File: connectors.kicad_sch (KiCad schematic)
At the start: 10 parts, among them J1 CE_Jumper, J2 LDO_EN, J3 Conn_01x05_Pin, J4 JST_VH_B2P_3.96mm, J5 JST_VH_B2P_3.96mm, J7 Thermistor_1, J8 Thermistor_2

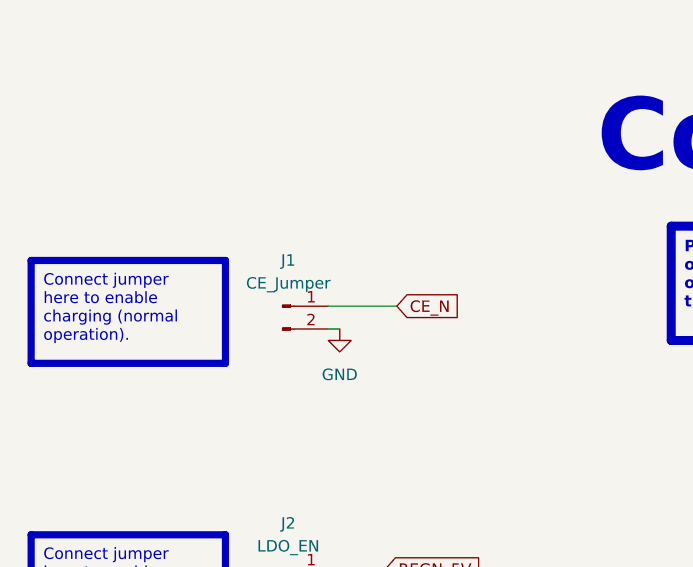
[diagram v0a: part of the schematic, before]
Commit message: Replace jumper to force BOM updated
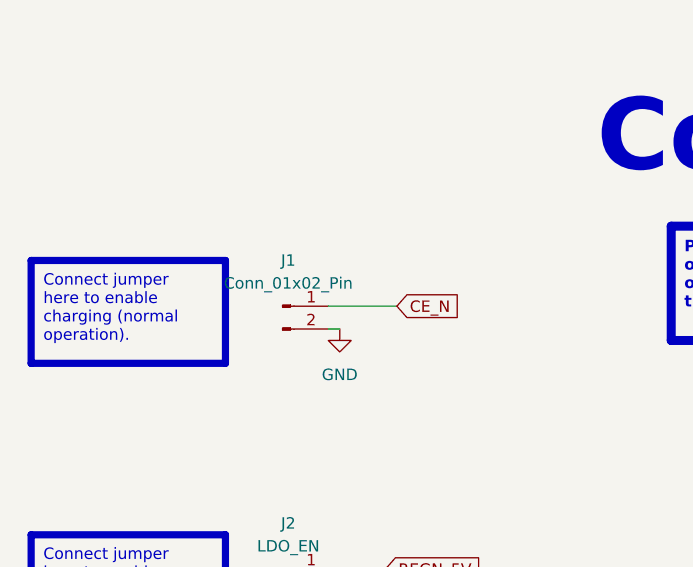
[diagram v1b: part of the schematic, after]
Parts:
- J1: value CE_Jumper -> Conn_01x02_Pin
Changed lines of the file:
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@@
-	)
-	(symbol
-		(lib_id "Connector:Conn_01x02_Pin")
-		(at 76.2 48.26 0)
-		(unit 1)
-		(exclude_from_sim no)
-		(in_bom yes)
-		(on_board yes)
-		(dnp no)
-		(fields_autoplaced yes)
-		(property "Reference" "J1"
-			(at 76.835 43.18 0)
-			(effects
-				(font
-					(size 1.27 1.27)
-				)
-			)
-		)
-		(property "Value" "CE_Jumper"
-			(at 76.835 45.72 0)
-			(effects
-				(font
-					(size 1.27 1.27)
-				)
-			)
-		)
-		(property "Footprint" "Connector_PinHeader_2.54mm:PinHeader_1x02_P2.54mm_Vertical"
-			(at 76.2 48.26 0)
-			(effects
-				(font
-					(size 1.27 1.27)
-				)
-				(hide yes)
-			)
-		)
-		(property "Datasheet" "~"
-			(at 76.2 48.26 0)
-			(effects
-				(font
-					(size 1.27 1.27)
-				)
-				(hide yes)
-			)
-		)
-		(property "Description" "Generic connector, single row, 01x02, script generated"
-			(at 76.2 48.26 0)
-			(effects
-				(font
-					(size 1.27 1.27)
-				)
-				(hide yes)
-			)
-		)
-		(pin "2"
-		)
-		(pin "1"
-		)
-		(instances
-			(project "solar_smart_station"
-				(path "/f9e05184-c88b-4a88-ae9c-ab2bdb32be7c/c5103ceb-5325-4a84-a025-9638a412984e/ae8d0caf-6898-4dee-88e6-fcc8a5387577"
-					(reference "J1")
-					(unit 1)
-				)
-			)
-		)
 	)
 	(symbol
@@
 					(unit 1)
 				)
+			)
+		)
+	)
+	(symbol
+		(lib_id "Connector:Conn_01x02_Pin")
+		(at 76.2 48.26 0)
+		(unit 1)
+		(exclude_from_sim no)
+		(in_bom yes)
+		(on_board yes)
+		(dnp no)
+		(fields_autoplaced yes)
+		(property "Reference" "J1"
+			(at 76.835 43.18 0)
+			(effects
+				(font
+					(size 1.27 1.27)
+				)
+			)
+		)
+		(property "Value" "Conn_01x02_Pin"
+			(at 76.835 45.72 0)
+			(effects
+				(font
+					(size 1.27 1.27)
+				)
+			)
+		)
+		(property "Footprint" "Connector_PinHeader_2.54mm:PinHeader_1x02_P2.54mm_Vertical"
+			(at 76.2 48.26 0)
+			(effects
+				(font
+					(size 1.27 1.27)
+				)
+				(hide yes)
+			)
+		)
+		(property "Datasheet" "~"
+			(at 76.2 48.26 0)
+			(effects
+				(font
+					(size 1.27 1.27)
+				)
+				(hide yes)
+			)
+		)
+		(property "Description" "Generic connector, single row, 01x02, script generated"
+			(at 76.2 48.26 0)
+			(effects
+				(font
+					(size 1.27 1.27)
+				)
+				(hide yes)
+			)
+		)
+		(pin "2"
+		)
+		(pin "1"
+		)
+		(instances
+			(project ""
+				(path "/f9e05184-c88b-4a88-ae9c-ab2bdb32be7c/c5103ceb-5325-4a84-a025-9638a412984e/ae8d0caf-6898-4dee-88e6-fcc8a5387577"
+					(reference "J1")
+					(unit 1)
+				)

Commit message: Finish checking - Ready for 1st release
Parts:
- renumbered J7 to J4, J8 to J5, J4 to JST1, J5 to JST2
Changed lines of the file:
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@@
 		(on_board yes)
 		(dnp no)
-		(property "Reference" "J8"
+		(property "Reference" "J5"
 			(at 184.785 110.49 0)
 			(effects
@@
 			(project "solar_smart_station"
 				(path "/f9e05184-c88b-4a88-ae9c-ab2bdb32be7c/c5103ceb-5325-4a84-a025-9638a412984e/ae8d0caf-6898-4dee-88e6-fcc8a5387577"
-					(reference "J8")
+					(reference "J5")
 					(unit 1)
 				)
@@
 		(dnp no)
 		(fields_autoplaced yes)
-		(property "Reference" "J5"
+		(property "Reference" "JST2"
 			(at 186.69 63.4999 0)
 			(effects
@@
 			(project "solar_smart_station"
 				(path "/f9e05184-c88b-4a88-ae9c-ab2bdb32be7c/c5103ceb-5325-4a84-a025-9638a412984e/ae8d0caf-6898-4dee-88e6-fcc8a5387577"
-					(reference "J5")
+					(reference "JST2")
 					(unit 1)
 				)
@@
 		(dnp no)
 		(fields_autoplaced yes)
-		(property "Reference" "#PWR045"
+		(property "Reference" "#PWR046"
 			(at 180.34 72.39 0)
 			(effects
@@
 			(project "solar_smart_station"
 				(path "/f9e05184-c88b-4a88-ae9c-ab2bdb32be7c/c5103ceb-5325-4a84-a025-9638a412984e/ae8d0caf-6898-4dee-88e6-fcc8a5387577"
-					(reference "#PWR045")
+					(reference "#PWR046")
 					(unit 1)
 				)
@@
 		(on_board yes)
 		(dnp no)
-		(property "Reference" "J7"
+		(property "Reference" "J4"
 			(at 184.785 97.79 0)
 			(effects
@@
 			(project "solar_smart_station"
 				(path "/f9e05184-c88b-4a88-ae9c-ab2bdb32be7c/c5103ceb-5325-4a84-a025-9638a412984e/ae8d0caf-6898-4dee-88e6-fcc8a5387577"
-					(reference "J7")
+					(reference "J4")
 					(unit 1)
 				)
@@
 		(dnp no)
 		(fields_autoplaced yes)
-		(property "Reference" "#PWR039"
+		(property "Reference" "#PWR041"
 			(at 82.55 57.15 0)
 			(effects
@@
 			(project "solar_smart_station"
 				(path "/f9e05184-c88b-4a88-ae9c-ab2bdb32be7c/c5103ceb-5325-4a84-a025-9638a412984e/ae8d0caf-6898-4dee-88e6-fcc8a5387577"
-					(reference "#PWR039")
+					(reference "#PWR041")
 					(unit 1)
 				)
@@
 		(dnp no)
 		(fields_autoplaced yes)
-		(property "Reference" "#PWR044"
+		(property "Reference" "#PWR045"
 			(at 180.34 54.61 0)
 			(effects
@@
 			(project "solar_smart_station"
 				(path "/f9e05184-c88b-4a88-ae9c-ab2bdb32be7c/c5103ceb-5325-4a84-a025-9638a412984e/ae8d0caf-6898-4dee-88e6-fcc8a5387577"
-					(reference "#PWR044")
+					(reference "#PWR045")
 					(unit 1)
 				)
@@
 		(dnp no)
 		(fields_autoplaced yes)
-		(property "Reference" "#PWR040"
+		(property "Reference" "#PWR042"
 			(at 152.4 49.53 0)
 			(effects
@@
 			(project "solar_smart_station"
 				(path "/f9e05184-c88b-4a88-ae9c-ab2bdb32be7c/c5103ceb-5325-4a84-a025-9638a412984e/ae8d0caf-6898-4dee-88e6-fcc8a5387577"
-					(reference "#PWR040")
+					(reference "#PWR042")
 					(unit 1)
 				)
@@
 		(dnp no)
 		(fields_autoplaced yes)
-		(property "Reference" "#PWR041"
+		(property "Reference" "#PWR047"
 			(at 209.55 50.8 0)
 			(effects
@@
 			(project "solar_smart_station"
 				(path "/f9e05184-c88b-4a88-ae9c-ab2bdb32be7c/c5103ceb-5325-4a84-a025-9638a412984e/ae8d0caf-6898-4dee-88e6-fcc8a5387577"
-					(reference "#PWR041")
+					(reference "#PWR047")
 					(unit 1)
 				)
@@
 		(dnp no)
 		(fields_autoplaced yes)
-		(property "Reference" "#PWR025"
+		(property "Reference" "#PWR039"
 			(at 60.96 138.43 0)
 			(effects
@@
 			(project "solar_smart_station"
 				(path "/f9e05184-c88b-4a88-ae9c-ab2bdb32be7c/c5103ceb-5325-4a84-a025-9638a412984e/ae8d0caf-6898-4dee-88e6-fcc8a5387577"
-					(reference "#PWR025")
+					(reference "#PWR039")
 					(unit 1)
 				)
@@
 		(on_board yes)
 		(dnp no)
-		(property "Reference" "#PWR047"
+		(property "Reference" "#PWR040"
 			(at 60.96 166.37 0)
 			(effects
@@
 			(project "solar_smart_station"
 				(path "/f9e05184-c88b-4a88-ae9c-ab2bdb32be7c/c5103ceb-5325-4a84-a025-9638a412984e/ae8d0caf-6898-4dee-88e6-fcc8a5387577"
-					(reference "#PWR047")
+					(reference "#PWR040")
 					(unit 1)
 				)
@@
 		(dnp no)
 		(fields_autoplaced yes)
-		(property "Reference" "#FLG03"
+		(property "Reference" "#FLG04"
 			(at 81.28 88.265 0)
 			(effects
@@
 			(project "solar_smart_station"
 				(path "/f9e05184-c88b-4a88-ae9c-ab2bdb32be7c/c5103ceb-5325-4a84-a025-9638a412984e/ae8d0caf-6898-4dee-88e6-fcc8a5387577"
-					(reference "#FLG03")
+					(reference "#FLG04")
 					(unit 1)
 				)
@@
 		(dnp no)
 		(fields_autoplaced yes)
-		(property "Reference" "#PWR042"
+		(property "Reference" "#PWR043"
 			(at 172.72 105.41 0)
 			(effects
@@
 			(project "solar_smart_station"
 				(path "/f9e05184-c88b-4a88-ae9c-ab2bdb32be7c/c5103ceb-5325-4a84-a025-9638a412984e/ae8d0caf-6898-4dee-88e6-fcc8a5387577"
-					(reference "#PWR042")
+					(reference "#PWR043")
 					(unit 1)
 				)
@@
 		(dnp no)
 		(fields_autoplaced yes)
-		(property "Reference" "#FLG01"
+		(property "Reference" "#FLG05"
 			(at 180.34 38.735 0)
 			(effects
@@
 			(project ""
 				(path "/f9e05184-c88b-4a88-ae9c-ab2bdb32be7c/c5103ceb-5325-4a84-a025-9638a412984e/ae8d0caf-6898-4dee-88e6-fcc8a5387577"
-					(reference "#FLG01")
+					(reference "#FLG05")
 					(unit 1)
 				)
@@
 		(dnp no)
 		(fields_autoplaced yes)
-		(property "Reference" "J4"
+		(property "Reference" "JST1"
 			(at 186.69 45.7199 0)
 			(effects
@@
 			(project "solar_smart_station"
 				(path "/f9e05184-c88b-4a88-ae9c-ab2bdb32be7c/c5103ceb-5325-4a84-a025-9638a412984e/ae8d0caf-6898-4dee-88e6-fcc8a5387577"
-					(reference "J4")
+					(reference "JST1")
 					(unit 1)
 				)
@@
 		(dnp no)
 		(fields_autoplaced yes)
-		(property "Reference" "#FLG02"
+		(property "Reference" "#FLG06"
 			(at 209.55 38.735 0)
 			(effects
@@
 			(project "solar_smart_station"
 				(path "/f9e05184-c88b-4a88-ae9c-ab2bdb32be7c/c5103ceb-5325-4a84-a025-9638a412984e/ae8d0caf-6898-4dee-88e6-fcc8a5387577"
-					(reference "#FLG02")
+					(reference "#FLG06")
 					(unit 1)
 				)
@@
 		(dnp no)
 		(fields_autoplaced yes)
-		(property "Reference" "#PWR043"
+		(property "Reference" "#PWR044"
 			(at 172.72 118.11 0)
 			(effects
@@
 			(project "solar_smart_station"
 				(path "/f9e05184-c88b-4a88-ae9c-ab2bdb32be7c/c5103ceb-5325-4a84-a025-9638a412984e/ae8d0caf-6898-4dee-88e6-fcc8a5387577"
-					(reference "#PWR043")
-					(unit 1)
-				)
+					(reference "#PWR044")
+					(unit 1)
+				)

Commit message: Ready for 1st release
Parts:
- JST1, JST2: value JST_VH_B2P_3.96mm -> Conn_01x02_Socket; MPN TBD -> (none)
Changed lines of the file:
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@@
-	)
-	(symbol
-		(lib_id "Connector:Conn_01x02_Socket")
-		(at 185.42 63.5 0)
-		(unit 1)
-		(exclude_from_sim no)
-		(in_bom yes)
-		(on_board yes)
-		(dnp no)
-		(fields_autoplaced yes)
-		(property "Reference" "JST2"
-			(at 186.69 63.4999 0)
-			(effects
-				(font
-					(size 1.27 1.27)
-				)
-				(justify left)
-			)
-		)
-		(property "Value" "JST_VH_B2P_3.96mm"
-			(at 186.69 66.0399 0)
-			(effects
-				(font
-					(size 1.27 1.27)
-				)
-				(justify left)
-			)
-		)
-		(property "Footprint" "Connector_JST:JST_VH_B2P-VH_1x02_P3.96mm_Vertical"
-			(at 185.42 63.5 0)
-			(effects
-				(font
-					(size 1.27 1.27)
-				)
-				(hide yes)
-			)
-		)
-		(property "Datasheet" "~"
-			(at 185.42 63.5 0)
-			(effects
-				(font
-					(size 1.27 1.27)
-				)
-				(hide yes)
-			)
-		)
-		(property "Description" "JST_VH_B2P_3.96mm"
-			(at 185.42 63.5 0)
-			(effects
-				(font
-					(size 1.27 1.27)
-				)
-				(hide yes)
-			)
-		)
-		(property "MPN" "TBD"
-			(at 185.42 63.5 0)
-			(effects
-				(font
-					(size 1.27 1.27)
-				)
-				(hide yes)
-			)
-		)
-		(pin "1"
-		)
-		(pin "2"
-		)
-		(instances
-			(project "solar_smart_station"
-				(path "/f9e05184-c88b-4a88-ae9c-ab2bdb32be7c/c5103ceb-5325-4a84-a025-9638a412984e/ae8d0caf-6898-4dee-88e6-fcc8a5387577"
-					(reference "JST2")
-					(unit 1)
-				)
-			)
-		)
 	)
 	(symbol
@@
 				(path "/f9e05184-c88b-4a88-ae9c-ab2bdb32be7c/c5103ceb-5325-4a84-a025-9638a412984e/ae8d0caf-6898-4dee-88e6-fcc8a5387577"
 					(reference "J3")
+					(unit 1)
+				)
+			)
+		)
+	)
+	(symbol
+		(lib_id "Connector:Conn_01x02_Socket")
+		(at 185.42 45.72 0)
+		(unit 1)
+		(exclude_from_sim no)
+		(in_bom yes)
+		(on_board yes)
+		(dnp no)
+		(fields_autoplaced yes)
+		(property "Reference" "JST1"
+			(at 186.69 45.7199 0)
+			(effects
+				(font
+					(size 1.27 1.27)
+				)
+				(justify left)
+			)
+		)
+		(property "Value" "Conn_01x02_Socket"
+			(at 186.69 48.2599 0)
+			(effects
+				(font
+					(size 1.27 1.27)
+				)
+				(justify left)
+			)
+		)
+		(property "Footprint" "Connector_JST:JST_VH_B2P-VH_1x02_P3.96mm_Vertical"
+			(at 185.42 45.72 0)
+			(effects
+				(font
+					(size 1.27 1.27)
+				)
+				(hide yes)
+			)
+		)
+		(property "Datasheet" "~"
+			(at 185.42 45.72 0)
+			(effects
+				(font
+					(size 1.27 1.27)
+				)
+				(hide yes)
+			)
+		)
+		(property "Description" "Generic connector, single row, 01x02, script generated"
+			(at 185.42 45.72 0)
+			(effects
+				(font
+					(size 1.27 1.27)
+				)
+				(hide yes)
+			)
+		)
+		(pin "1"
+		)
+		(pin "2"
+		)
+		(instances
+			(project ""
+				(path "/f9e05184-c88b-4a88-ae9c-ab2bdb32be7c/c5103ceb-5325-4a84-a025-9638a412984e/ae8d0caf-6898-4dee-88e6-fcc8a5387577"
+					(reference "JST1")
 					(unit 1)
 				)
@@
 	(symbol
 		(lib_id "Connector:Conn_01x02_Socket")
-		(at 185.42 45.72 0)
-		(unit 1)
-		(exclude_from_sim no)
-		(in_bom yes)
-		(on_board yes)
-		(dnp no)
-		(fields_autoplaced yes)
-		(property "Reference" "JST1"
-			(at 186.69 45.7199 0)
+		(at 185.42 63.5 0)
+		(unit 1)
+		(exclude_from_sim no)
+		(in_bom yes)
+		(on_board yes)
+		(dnp no)
+		(fields_autoplaced yes)
+		(property "Reference" "JST2"
+			(at 186.69 63.4999 0)
 			(effects
 				(font
@@
 			)
 		)
-		(property "Value" "JST_VH_B2P_3.96mm"
-			(at 186.69 48.2599 0)
+		(property "Value" "Conn_01x02_Socket"
+			(at 186.69 66.0399 0)
 			(effects
 				(font
@@
 		)
 		(property "Footprint" "Connector_JST:JST_VH_B2P-VH_1x02_P3.96mm_Vertical"
-			(at 185.42 45.72 0)
+			(at 185.42 63.5 0)
 			(effects
 				(font
@@
 		)
 		(property "Datasheet" "~"
-			(at 185.42 45.72 0)
-			(effects
-				(font
-					(size 1.27 1.27)
-				)
-				(hide yes)
-			)
-		)
-		(property "Description" "JST_VH_B2P_3.96mm"
-			(at 185.42 45.72 0)
-			(effects
-				(font
-					(size 1.27 1.27)
-				)
-				(hide yes)
-			)
-		)
-		(property "MPN" "TBD"
-			(at 185.42 45.72 0)
+			(at 185.42 63.5 0)
+			(effects
+				(font
+					(size 1.27 1.27)
+				)
+				(hide yes)
+			)
+		)
+		(property "Description" "Generic connector, single row, 01x02, script generated"
+			(at 185.42 63.5 0)
 			(effects
 				(font
@@
 		)
 		(instances
-			(project "solar_smart_station"
-				(path "/f9e05184-c88b-4a88-ae9c-ab2bdb32be7c/c5103ceb-5325-4a84-a025-9638a412984e/ae8d0caf-6898-4dee-88e6-fcc8a5387577"
-					(reference "JST1")
-					(unit 1)
-				)
+			(project ""
+				(path "/f9e05184-c88b-4a88-ae9c-ab2bdb32be7c/c5103ceb-5325-4a84-a025-9638a412984e/ae8d0caf-6898-4dee-88e6-fcc8a5387577"
+					(reference "JST2")
+					(unit 1)
+				)
